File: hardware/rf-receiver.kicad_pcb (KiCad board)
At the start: 4 copper layers, 90.8 x 50 mm, 160 parts, among them CON1 FPC_6POS, IC1 ATSAMD21G18A-AU, IC2 AD9954, IC3 74LVC74, J1 Conn_01x05_Female, J2 Conn_Coaxial, J3 USB_C_Receptacle, P1 ROT_ENC, SW1 BTN1, SW2 BTN2, SW3 BTN3, U1 74HC14, U10 TPS62173DSG, U11 MIC5504-1.8YM5, U12 MIC5504-1.8YM5, U2 RC1602A, U3 TXB0108PWR, U4 MIC5504-3.3YM5, U5 OPA300, U7 Transformer, U8 NE5532, U9 74CBTLV3253, Y1 Crystal_Small

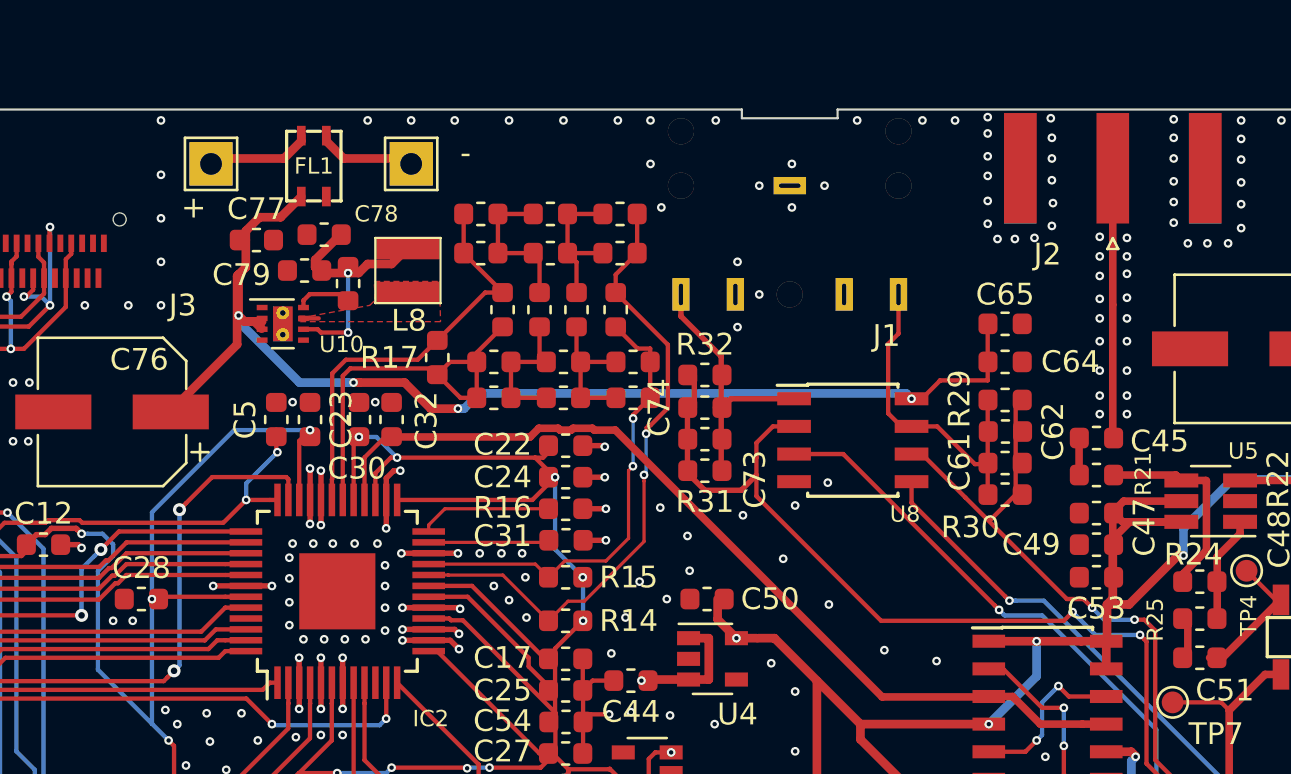
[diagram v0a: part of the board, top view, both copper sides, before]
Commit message: Finished work on Receiver RPi shield. Changed CLK to SI5351A. Minimized footprints for almost all Tayloe detector ICs. Added -12V to audio opamps. Prepared board for coexisting with Hifiberry.
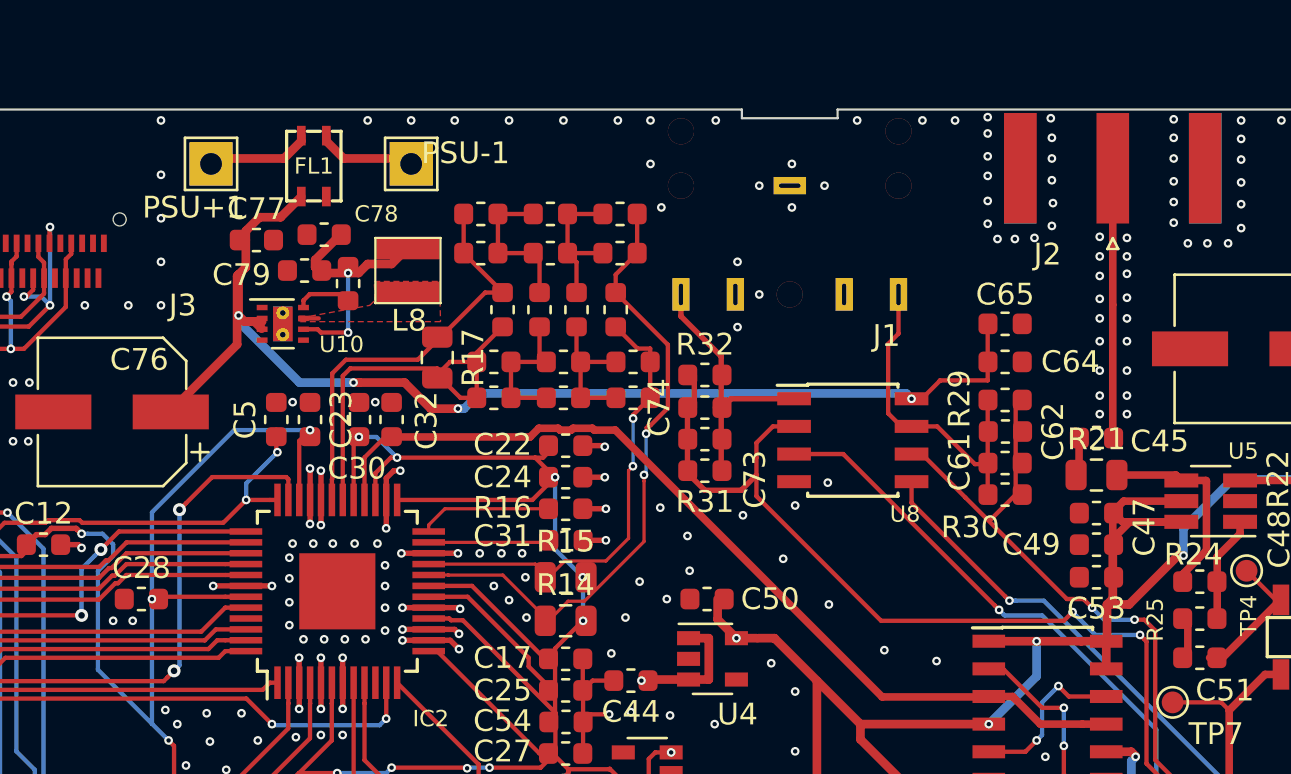
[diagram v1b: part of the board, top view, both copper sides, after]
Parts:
- R14, R15, R17, R21: footprint Resistor_SMD:R_0603_1608Metric -> Resistor_SMD:R_0805_2012Metric
- renumbered + to PSU+1, - to PSU-1
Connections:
- C43 pad 1: /JTAGConn58895F8D/MCU_RESET -> /UART_TX
- CON1 pad 4: /UART_TX -> /JTAGConn58895F8D/MCU_RESET
- CON1 pad 5: /JTAGConn58895F8D/MCU_RESET -> /UART_TX
- CON1 pad 7: (no net) -> Net-(CON1-Pad7)
- R18 pad 2: /JTAGConn58895F8D/MCU_RESET -> /UART_TX

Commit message: Added rpi changes - seems weird that I forgot that for so long
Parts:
- removed C24, C25, C26, C27, C28, C29, C30, C43, C54, C77, C79, C80, C82: 100nF, Capacitor_SMD:C_0603_1608Metric
- removed C31: 1uF, Capacitor_SMD:C_0603_1608Metric
- removed C32, C33, C37, C38: 22pF, Capacitor_SMD:C_0603_1608Metric
- removed C34, C35, C39: 39pF, Capacitor_SMD:C_0603_1608Metric
- removed C36, C42: 33pF, Capacitor_SMD:C_0603_1608Metric
- removed C40, C41: 7.5pF, Capacitor_SMD:C_0603_1608Metric
- removed C55: C_Small, Capacitor_SMD:C_0603_1608Metric
- removed C76: 100uF, Capacitor_SMD:CP_Elec_6.3x7.7
- removed C78: 22uF, Capacitor_SMD:C_0603_1608Metric
- removed C83, C85: 10uF, Capacitor_SMD:C_0603_1608Metric
- removed CON1: FPC_6POS, FPC_conn:HFW6R_2STE1LF
- removed IC1: ATSAMD21G18A-AU, Package_QFP:TQFP-48_7x7mm_P0.5mm
- removed IC2: AD9954, Package_QFP:TQFP-48-1EP_7x7mm_P0.5mm_EP3.5x3.5mm
- removed L2, L3: 12nH, Inductor_SMD:L_0603_1608Metric
- removed L4, L5: 18nH, Inductor_SMD:L_0603_1608Metric
- removed L6, L7: 20nH, Inductor_SMD:L_0603_1608Metric
- removed L8: 2.2uH, athir:XFL3012
- removed PSU+1: PSU+, TestPoint:TestPoint_THTPad_2.0x2.0mm_Drill1.0mm
- removed PSU-1: PSU-, TestPoint:TestPoint_THTPad_2.0x2.0mm_Drill1.0mm
- removed R10, R30, R32: 10kohm, Resistor_SMD:R_0603_1608Metric
- removed R11: 220ohm, Resistor_SMD:R_0603_1608Metric
- removed R12: 2kohm, Resistor_SMD:R_0603_1608Metric
- removed R13: 243ohm, Resistor_SMD:R_0603_1608Metric
- removed R14, R15, R17: 50ohm, Resistor_SMD:R_0805_2012Metric
- removed R16: 3.92kohm, Resistor_SMD:R_0603_1608Metric
- removed R18, R19, R20: 100kohm, Resistor_SMD:R_0603_1608Metric
- removed R33: 100k, Resistor_SMD:R_0603_1608Metric
- removed SW1: BTN1, Connector_PinHeader_2.54mm:PinHeader_1x02_P2.54mm_Vertical
- removed SW2: BTN2, Connector_PinHeader_2.54mm:PinHeader_1x02_P2.54mm_Vertical
- removed SW3: BTN3, Connector_PinHeader_2.54mm:PinHeader_1x02_P2.54mm_Vertical
- removed U10: TPS62173DSG, Package_SON:WSON-8-1EP_2x2mm_P0.5mm_EP0.9x1.6mm_ThermalVias
- removed U11, U12: MIC5504-1.8YM5, Package_TO_SOT_SMD:SOT-23-5
- removed W1: TX, TestPoint:TestPoint_THTPad_2.0x2.0mm_Drill1.0mm
- removed W2: RX, TestPoint:TestPoint_THTPad_2.0x2.0mm_Drill1.0mm
- removed XTAL1: 25MHz 20pF, Crystal:Crystal_SMD_3225-4Pin_3.2x2.5mm
- added D1: LED, Diode_SMD:D_1206_3216Metric, F.Cu at (89.8, 105.8)
- added D2: LED, Diode_SMD:D_1206_3216Metric, F.Cu at (89.8, 108.5)
- added D3: D_Small_ALT, Diode_SMD:D_SOD-323_HandSoldering, F.Cu at (118.5, 117.3)
- added FL2: ACP3225, athir:ACP3225, F.Cu at (122.3, 85.5)
- added FL3: ACP3225, athir:ACP3225, F.Cu at (122.0, 94.6)
- added J10: 12P_VIN, athir:FASTON63951-1, F.Cu at (124.0, 81.0)
- added J12: 12N_VIN, athir:FASTON63951-1, F.Cu at (124.0, 90.5)
- added J4: 5_VIN, athir:FASTON63951-1, F.Cu at (122.6, 116.0)
- added J5: RF_Shield_One_Piece, RF_Shielding:Laird_Technologies_BMI-S-102_16.50x16.50mm, F.Cu at (112.2, 67.2)
- added J6: RF_Shield_One_Piece, RF_Shielding:Laird_Technologies_BMI-S-101_13.66x12.70mm, F.Cu at (112.0, 85.5)
- added J7: RF_Shield_One_Piece, RF_Shielding:Laird_Technologies_BMI-S-102_16.50x16.50mm, F.Cu at (92.0, 90.0)
- added J8: RF_Shield_One_Piece, RF_Shielding:Laird_Technologies_BMI-S-101_13.66x12.70mm, F.Cu at (92.0, 65.8)
- added J9: GND_IN, athir:FASTON63951-1, F.Cu at (114.5, 116.0)
- added JP1: Jumper_2_Open, Connector_PinHeader_2.54mm:PinHeader_1x02_P2.54mm_Vertical, F.Cu at (129.2, 99.0)
- added REF**: RPIHAT, athir:RPIHAT, F.Cu at (103.2, 90.2)
- added TP1: RF_DC_BIAS, athir:testpoint_probe, F.Cu at (101.5, 67.0)
- added TP10: 5V_TP, athir:testpoint_probe, F.Cu at (84.2, 101.3)
- added TP11: 12V_TP, athir:testpoint_probe, F.Cu at (110.5, 96.0)
- added TP12: -12V_TP, athir:testpoint_probe, F.Cu at (105.2, 95.0)
- added TP13: SCL, athir:testpoint_probe, F.Cu at (83.2, 66.2)
- added TP14: 3.3VA, athir:testpoint_probe, F.Cu at (83.2, 73.8)
- added TP15: 3.3V, athir:testpoint_probe, F.Cu at (110.0, 107.5)
- added TP2: SDA, athir:testpoint_probe, F.Cu at (83.2, 60.5)
- added TP9: GND, athir:testpoint_probe, F.Cu at (91.2, 101.2)
- C1, C2: value 15pF -> DC BLOCK
- C10, C9: value 0.1uF -> 22uF; footprint Capacitor_SMD:C_0603_1608Metric -> Capacitor_SMD:C_0805_2012Metric
- C11: value 10uF -> 22uF; footprint Capacitor_SMD:C_0603_1608Metric -> Capacitor_SMD:C_0805_2012Metric
- C13: value 10uF -> 100nF
- C14, C15: value 100nF -> 39pF
- C18, C44, C5: value 100nF -> 10uF
- C19: value 10nF -> 10uF
- C20, C21: value 39pF -> 100nF
- C52: value 47uF -> 22uF; footprint Capacitor_SMD:CP_Elec_6.3x7.7 -> Capacitor_SMD:C_0805_2012Metric
- C56: footprint Capacitor_SMD:C_0603_1608Metric -> Capacitor_SMD:CP_Elec_4x5.4
- C6: value 100nF -> 10nF
- C7: value 100nF -> 22uF; footprint Capacitor_SMD:C_0603_1608Metric -> Capacitor_SMD:C_0805_2012Metric
- C8: value 100nF -> 47uF/100uF; footprint Capacitor_SMD:C_0603_1608Metric -> Capacitor_SMD:CP_Elec_6.3x5.4
- FL1: value ACP3225 -> ACM90V-701-2PL-TL00; footprint athir:ACP3225 -> athir:ACM70V-701-2PL-TL00
- IC3: value 74LVC74 -> 74LVC74ABQ; footprint Package_SO:SOIC-14_3.9x8.7mm_P1.27mm -> athir:DHVQFN14
- J1: value Conn_01x05_Female -> InputConP6; footprint athir:SJ1-35235 -> Connector_PinSocket_2.54mm:PinSocket_1x05_P2.54mm_Vertical
- J3: value USB_C_Receptacle -> Raspberry_Pi_2_3; footprint athir:DX07S024JJ -> Connector_PinSocket_2.54mm:PinSocket_2x20_P2.54mm_Vertical; moved to B.Cu
- L1: value SMD-FERRITE-CHIP-120-OHM-500MA_0603_ -> 47+uH; footprint Capacitor_SMD:C_0603_1608Metric -> Inductor_SMD:L_Wuerth_HCM-7050
- R3: value R_Small -> 100; footprint Resistor_SMD:R_0603_1608Metric -> Resistor_SMD:R_0805_2012Metric
- R4: value R_Small -> 1k
- R5, R8: value 10kohm -> 3k9
- R6, R7: value 10kohm -> I2CPULLUP
- R9: value 10kohm -> 100; footprint Resistor_SMD:R_0603_1608Metric -> Resistor_SMD:R_0805_2012Metric
- TP3, TP4, TP5, TP6, TP7, TP8: footprint TestPoint:TestPoint_Pad_D1.0mm -> athir:testpoint_probe
- U1: value 74HC14 -> MIC5504-3.3YM5; footprint Package_SO:TSSOP-14_4.4x5mm_P0.65mm -> Package_TO_SOT_SMD:SOT-23-5
- U2: value RC1602A -> CAT24C128; footprint Connector_PinHeader_2.54mm:PinHeader_1x16_P2.54mm_Vertical -> Package_SO:SOIC-8_3.9x4.9mm_P1.27mm
- U3: value TXB0108PWR -> SI5351A-B-GT; footprint Package_SO:TSSOP-20_4.4x6.5mm_P0.65mm -> digikey-footprints:MSOP-10_W3mm
- U8: value NE5532 -> OPA167B-DRG; footprint Package_SO:SOIC-8_3.9x4.9mm_P1.27mm -> Package_SON:SON-8-1EP_3x2mm_P0.5mm_EP1.4x1.6mm
- U9: footprint Package_SO:TSSOP-16_4.4x5mm_P0.65mm -> athir:PVQFN16
- Y1: value Crystal_Small -> 25MHz 20pF; footprint Crystal:Crystal_SMD_3215-2Pin_3.2x1.5mm -> Crystal:Crystal_SMD_3225-4Pin_3.2x2.5mm
- moved U9 80.0 mm to (68.8, 91.2)
- moved C66 69.7 mm to (86.2, 83.5), turned to 180 degrees
- moved C67 69.7 mm to (86.2, 85.2), turned to 180 degrees
- moved C68 69.7 mm to (86.2, 87.2), turned to 180 degrees
- moved C69 69.6 mm to (86.2, 89.0), turned to 180 degrees
- moved C70 69.6 mm to (86.2, 91.0), turned to 180 degrees
- moved C71 69.5 mm to (86.2, 92.8), turned to 180 degrees
- moved C72 69.5 mm to (86.2, 94.8), turned to 180 degrees
- moved C75 69.5 mm to (86.2, 96.5), turned to 180 degrees
- moved R6 69.2 mm to (87.0, 62.5), turned to 270 degrees
- moved R7 60.8 mm to (88.8, 62.5), turned to 270 degrees
- moved C7 58.3 mm to (84.5, 111.5), turned to 90 degrees
- moved TP8 57.6 mm to (86.9, 101.2), turned to 180 degrees
- moved R9 57.4 mm to (85.2, 108.5), turned to 0 degrees
- moved C56 56.9 mm to (96.0, 76.2)
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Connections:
- C1 pad 1: Net-(C1-Pad1) -> /I_OUT
- C1 pad 2: GND -> /right
- C10 pad 1: +5V -> Net-(C10-Pad1)
- C10 pad 2: GND -> Net-(C10-Pad2)
- C11 pad 1: +1V8 -> Net-(C11-Pad1)
- C12 pad 1: +1V8 -> Net-(C12-Pad1)
- C12 pad 2: GND -> Net-(C10-Pad2)
- C13 pad 1: /VDDANA -> Net-(C10-Pad1)
- C13 pad 2: GND -> Net-(C10-Pad2)
- C14 pad 1: +1V8 -> GND
- C14 pad 2: GND -> Net-(C14-Pad2)
- C15 pad 1: /VDDANA -> GND
- C15 pad 2: GND -> Net-(C15-Pad2)
- C16 pad 1: /VDDCORE -> +3.3VA
- C17 pad 2: VAA -> +3.3VA
- C18 pad 1: GND -> +5V
- C18 pad 2: +1V8 -> GND
- C19 pad 1: Net-(C19-Pad1) -> +3.3VA
- C19 pad 2: +1V8 -> GND
- C2 pad 1: Net-(C2-Pad1) -> /Q_OUT
- C2 pad 2: GND -> /left
- C20 pad 1: GND -> +3.3VA
- C20 pad 2: Net-(C20-Pad2) -> GND
- C21 pad 1: Net-(C21-Pad1) -> +3V3
- C22 pad 1: GND -> Net-(C11-Pad1)
- C22 pad 2: VAA -> GND
- C23 pad 2: +1V8 -> +3V3
- C5 pad 1: /DDS_RESET -> GND
- C5 pad 2: GND -> -12V
- C6 pad 1: Net-(C6-Pad1) -> GND
- C6 pad 2: GND -> -12V
- C61 pad 1: /Tayoe Mixer sheet/I_OUT -> /I_OUT
- C62 pad 1: /Tayoe Mixer sheet/I_OUT -> /I_OUT
- C7 pad 1: Net-(C7-Pad1) -> +5V
- C73 pad 1: /Tayoe Mixer sheet/Q_OUT -> /Q_OUT
- C74 pad 1: /Tayoe Mixer sheet/Q_OUT -> /Q_OUT
- C8 pad 1: Net-(C8-Pad1) -> Net-(C11-Pad1)
- C9 pad 1: +1V8 -> Net-(C12-Pad1)
- C9 pad 2: GND -> Net-(C10-Pad2)
- FL1 pad 1: +12V -> Net-(C10-Pad2)
- FL1 pad 2: GND -> Net-(D3-Pad1)
- FL1 pad 3: Net-(FL1-Pad3) -> Net-(C11-Pad1)
- FL1 pad 4: Net-(FL1-Pad4) -> GND
- IC3 pad 11: /AD9954sheet/COMP_OUT -> /Tayoe Mixer sheet/LO_IN
- IC3 pad 3: /AD9954sheet/COMP_OUT -> /Tayoe Mixer sheet/LO_IN
- J1 pad 1: GND -> /right
- J1 pad 2: /Tayoe Mixer sheet/Q_OUT -> (no net)
- J1 pad 3: /Tayoe Mixer sheet/I_OUT -> GND
- J1 pad 4: GND -> (no net)
- J1 pad 5: Net-(J1-Pad5) -> /left
- L1 pad 1: +1V8 -> Net-(C11-Pad1)
- L1 pad 2: /VDDANA -> +5V
- R29 pad 1: /Tayoe Mixer sheet/I_OUT -> /I_OUT
- R3 pad 1: /USB_VCC -> Net-(J3-Pad32)
- R3 pad 2: Net-(C55-Pad1) -> Net-(D1-Pad2)
- R31 pad 1: /Tayoe Mixer sheet/Q_OUT -> /Q_OUT
- R4 pad 1: /USB_VCC -> +3V3
- R4 pad 2: GND -> Net-(JP1-Pad1)
- R5 pad 2: Net-(R5-Pad2) -> /SCL
- R6 pad 1: +3V3 -> +3.3VA
- R6 pad 2: Net-(R6-Pad2) -> /SCL
- R7 pad 1: +3V3 -> +3.3VA
- R7 pad 2: Net-(R10-Pad1) -> /SDA
- R8 pad 1: Net-(R5-Pad2) -> +3V3
- R8 pad 2: Net-(C6-Pad1) -> /SDA
- R9 pad 1: Net-(R6-Pad2) -> Net-(J3-Pad33)
- R9 pad 2: Net-(C7-Pad1) -> Net-(D2-Pad2)
- U1 pad 1: Net-(C6-Pad1) -> +5V
- U1 pad 2: /BTN1 -> GND
- U1 pad 3: Net-(C8-Pad1) -> +5V
- U1 pad 4: /BTN3 -> (no net)
- U1 pad 5: Net-(C7-Pad1) -> +3.3VA
- U2 pad 2: +5V -> GND
- U2 pad 3: Net-(R12-Pad1) -> GND
- U2 pad 4: Net-(U2-Pad4) -> GND
- U2 pad 5: Net-(U2-Pad5) -> /SDA
- U2 pad 6: Net-(U2-Pad6) -> /SCL
- U2 pad 7: Net-(U2-Pad7) -> Net-(JP1-Pad1)
- U2 pad 8: Net-(U2-Pad8) -> +3V3
- U3 pad 1: /LCD_RS -> +3.3VA
- U3 pad 10: +1V8 -> /Tayoe Mixer sheet/LO_IN
- U3 pad 2: +1V8 -> Net-(C15-Pad2)
- U3 pad 3: /LCD_RW -> Net-(C14-Pad2)
- U3 pad 4: /LCD_EN -> /SCL
- U3 pad 5: /LCD_D4 -> /SDA
- U3 pad 6: /LCD_D5 -> (no net)
- U3 pad 7: /LCD_D6 -> +3.3VA
- U3 pad 8: /LCD_D7 -> GND
- U3 pad 9: Net-(U3-Pad9) -> (no net)
- U4 pad 4: Net-(U4-Pad4) -> (no net)
- U8 pad 1: /Tayoe Mixer sheet/Q_OUT -> /Q_OUT
- U8 pad 4: GND -> -12V
- U8 pad 7: /Tayoe Mixer sheet/I_OUT -> /I_OUT
- Y1 pad 1: Net-(C1-Pad1) -> Net-(C15-Pad2)
- Y1 pad 2: Net-(C2-Pad1) -> GND
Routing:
- net +1V8: track 168.2 -> 0.00 mm, vias 11 -> 0
- net /SDA: track 0.00 -> 133.2 mm, vias 0 -> 5
- net /SCL: track 0.00 -> 127.4 mm, vias 0 -> 7
- net VAA: track 107.1 -> 0.00 mm, vias 9 -> 0
- net /BTN3: track 68.0 -> 0.00 mm, vias 4 -> 0
- net /BTN2: track 67.0 -> 0.00 mm, vias 4 -> 0
- net /BTN1: track 61.7 -> 0.00 mm, vias 2 -> 0
- net Net-(C10-Pad2): track 0.00 -> 58.3 mm, vias 0 -> 1
- net +3.3VA: track 0.00 -> 52.2 mm, vias 0 -> 4
- net /AD9954sheet/COMP_OUT: track 42.4 -> 0.00 mm
- net Net-(J3-Pad33): track 0.00 -> 39.5 mm, vias 0 -> 1
- net /JTAGConn58895F8D/SWDIO: track 36.0 -> 0.00 mm, vias 2 -> 0
- net /UART_TX: track 35.9 -> 0.00 mm, vias 2 -> 0
- net /JTAGConn58895F8D/SWCLK: track 35.3 -> 0.00 mm, vias 2 -> 0
- net Net-(J3-Pad32): track 0.00 -> 33.8 mm, vias 0 -> 1
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- removed copper zone on F.Cu, net Net-(L8-Pad1)
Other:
- board size 90.8 x 50 mm -> 56.5 x 65 mm
- net class PWR: via_dia 0.6 -> 1.5; via_drill 0.4 -> 1
- net class PWR_1 added: clearance 0.15, trace_width 0.3, via_dia 0.6, via_drill 0.3
- net class RF added: clearance 0.15, trace_width 0.2, via_dia 0.45, via_drill 0.2
- board text added: "+12V"
- board text added: "+5V"
- board text added: "-12V"
- board text added: "AUDIO AMPS"
- board text added: "BUFFER 1:4 BALUN"
- board text added: "CLOCK"
- board text added: "Detector"
- board text added: "GND"
- board text added: "RF SHIELD 1950 - AT"
- board text removed: "RF Receiver 1912- AT"

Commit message: HW: Fixed SMA footprint and 74x3253 footprint
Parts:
- added TP16: TestPoint, athir:testpoint_probe, F.Cu at (92.3, 79.6)
- added TP17: TestPoint, athir:testpoint_probe, F.Cu at (97.7, 79.5)
- J2: footprint Connector_Coaxial:SMA_Amphenol_132289_EdgeMount -> athir:SMA_Edge-mount
- moved U9 22.7 mm to (91.4, 90.3)
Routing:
- net /Tayoe Mixer sheet/LO_IN_B: track 24.0 -> 31.3 mm, vias 1 -> 3
- net /Tayoe Mixer sheet/LO_IN: track 26.8 -> 30.1 mm
- net /Tayoe Mixer sheet/RF_B: track 35.8 -> 38.9 mm, vias 3 -> 5
- net /Tayoe Mixer sheet/RF_A: track 41.5 -> 44.0 mm
- net /Tayoe Mixer sheet/90_deg: track 33.9 -> 36.0 mm, vias 6 -> 7
- net /Tayoe Mixer sheet/180_deg: track 42.0 -> 43.6 mm, vias 5 -> 6
- net GND: track 37.6 -> 36.7 mm, vias 572 -> 569
- net /Tayoe Mixer sheet/270_deg: track 39.5 -> 40.3 mm, vias 5 -> 7
- net /Tayoe Mixer sheet/RF_IN_A: track 15.9 -> 16.6 mm
- net /Tayoe Mixer sheet/RF_BUFFERED: track 12.8 -> 13.3 mm
- net /Tayoe Mixer sheet/0_deg: track 37.1 -> 37.6 mm, vias 3 -> 4
- net /Tayoe Mixer sheet/LO_IN_A: track 22.0 -> 22.1 mm, vias 2 -> 3
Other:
- board text added: "RF SHIELD AT 2009"
- board text removed: "RF SHIELD 1950 - AT"

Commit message: Sorry future me
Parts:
- added C24: 330p, Capacitor_SMD:C_0603_1608Metric, F.Cu at (115.6, 72.9)
- added C25: 39p, Capacitor_SMD:C_0603_1608Metric, F.Cu at (122.2, 75.2)
- added C26: 330p, Capacitor_SMD:C_0603_1608Metric, F.Cu at (117.2, 72.9)
- added C27: 220p, Capacitor_SMD:C_0603_1608Metric, F.Cu at (122.2, 70.8)
- added C28: 270p, Capacitor_SMD:C_0603_1608Metric, F.Cu at (118.8, 72.9)
- added C29: 130p, Capacitor_SMD:C_0603_1608Metric, F.Cu at (122.1, 66.2)
- added C30: 270p, Capacitor_SMD:C_0603_1608Metric, F.Cu at (122.2, 62.5)
- added C31: 22uF, Capacitor_SMD:C_0805_2012Metric, F.Cu at (86.9, 111.5)
- added C32: 100nF, Capacitor_SMD:C_0603_1608Metric, F.Cu at (89.0, 111.5)
- added C33: 47uF/100uF, Capacitor_SMD:CP_Elec_6.3x5.4, F.Cu at (96.6, 103.1)
- added D4: D_Small_ALT, athir:SOD128, F.Cu at (119.4, 117.4)
- added JP2: SolderJumper_2_Open, Jumper:SolderJumper-2_P1.3mm_Open_TrianglePad1.0x1.5mm, F.Cu at (127.0, 77.9)
- added L2: 180n, Inductor_SMD:L_0805_2012Metric, F.Cu at (124.2, 75.2)
- added L3: 100n, Inductor_SMD:L_0805_2012Metric, F.Cu at (124.2, 70.8)
- added L4: 120n, Inductor_SMD:L_0805_2012Metric, F.Cu at (124.2, 66.2)
- added R10: 50ohm, Resistor_SMD:R_0603_1608Metric, F.Cu at (96.0, 70.2)
- added REF**: OSHW-Symbol_8.9x8mm_SilkScreen, Symbol:OSHW-Symbol_8.9x8mm_SilkScreen, B.Cu at (88.1, 117.8)
- added REF**: KiCad-Logo2_5mm_SilkScreen, Symbol:KiCad-Logo2_5mm_SilkScreen, B.Cu at (103.3, 113.5)
- added TP18: GND, athir:testpoint_probe, F.Cu at (109.2, 94.9)
- added TP19: RF_POST_LP, athir:testpoint_probe, F.Cu at (123.4, 59.6)
- added TP20: TestPoint, athir:testpoint_probe, F.Cu at (83.2, 71.5)
- added TP21: TestPoint, athir:testpoint_probe, F.Cu at (83.2, 68.5)
- C53, C63: value 0.1uF -> 100nF
- J2: value Conn_Coaxial -> ANT; moved to B.Cu
- MH1, MH2, MH3, MH4: footprint MountingHole:MountingHole_2.7mm_M2.5_Pad -> MountingHole:MountingHole_3.2mm_M3_Pad
- U6: renamed from IC3; footprint athir:DHVQFN14 -> athir:74LVC74ABQ
- moved TP5 19.9 mm to (102.4, 82.5)
- moved TP3 15.5 mm to (111.0, 77.2)
- moved TP4 8.79 mm to (114.9, 77.2)
- moved U6 6.68 mm to (96.5, 92.4)
- moved TP11 2.46 mm to (112.7, 94.9)
- moved U9 1.60 mm to (91.4, 88.7), turned to 90 degrees
- moved D3 1.45 mm to (117.0, 117.3)
- moved TP9 1.32 mm to (89.9, 101.4)
- moved TP14 1.15 mm to (83.2, 74.9)
- moved TP2 1.15 mm to (83.2, 59.4)
- moved TP13 1.00 mm to (83.2, 65.2)
- moved C8 0.60 mm to (96.2, 112.3)
- moved J9 0.60 mm to (113.9, 116.0)
- moved TP8 0.29 mm to (87.0, 101.4)
- moved U7 0.25 mm to (111.8, 71.6)
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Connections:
- J2 pad 1: /Tayoe Mixer sheet/RF_IN_A -> /Tayoe Mixer sheet/30 MHz Low Pass Filter/IN
- U3 pad 6: (no net) -> Net-(TP21-Pad1)
- U3 pad 9: (no net) -> Net-(TP20-Pad1)
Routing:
- net /Tayoe Mixer sheet/30 MHz Low Pass Filter/IN: track 0.00 -> 24.7 mm, vias 0 -> 1
- net +5V: track 58.8 -> 79.2 mm, vias 12 -> 13
- net Net-(C25-Pad1): track 0.00 -> 20.2 mm, vias 0 -> 2
- net /Tayoe Mixer sheet/RF_IN_A: track 16.6 -> 31.8 mm, vias 0 -> 1
- net Net-(C27-Pad1): track 0.00 -> 14.4 mm
- net /Tayoe Mixer sheet/LO_IN_B: track 31.3 -> 17.0 mm, vias 3 -> 1
- net /Tayoe Mixer sheet/LO_IN: track 30.1 -> 41.7 mm, vias 2 -> 4
- net +3V3: track 164.3 -> 156.0 mm, vias 12 -> 11
- net Net-(TP20-Pad1): track 0.00 -> 8.04 mm, vias 0 -> 1
- net Net-(TP21-Pad1): track 0.00 -> 7.54 mm, vias 0 -> 1
- net GND: track 36.7 -> 42.9 mm, vias 569 -> 509
- net /Tayoe Mixer sheet/180_deg: track 43.6 -> 38.2 mm, vias 6 -> 5
- net /Tayoe Mixer sheet/RF_B: track 38.9 -> 34.2 mm, vias 5 -> 3
- net /SDA: track 133.2 -> 128.8 mm, vias 5 -> 7
- net /Tayoe Mixer sheet/0_deg: track 37.6 -> 33.2 mm, vias 4 -> 2
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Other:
- board text added: "RF SHIELD 20AT13"
- board text removed: "RF SHIELD AT 2009"
